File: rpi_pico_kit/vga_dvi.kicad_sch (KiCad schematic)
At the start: 21 parts, among them J4 DB15_Female_HighDensity_Mount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, J5 HDMI_A

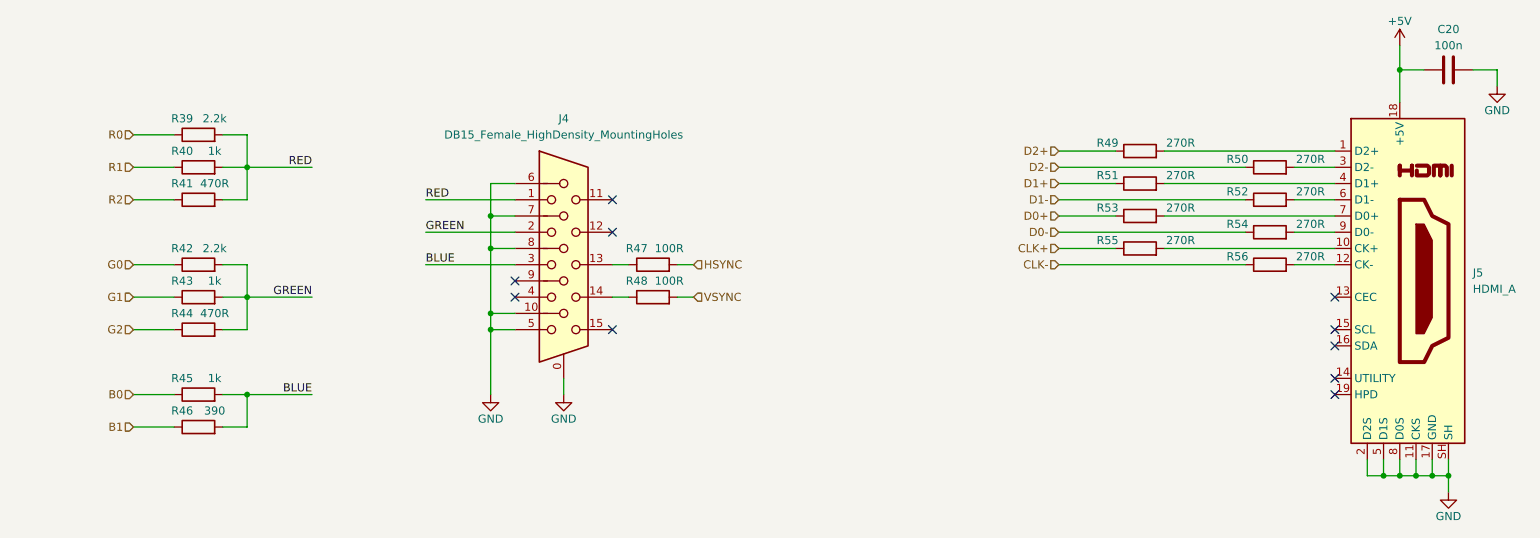
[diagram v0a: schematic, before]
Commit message: added i2c interface for vga and dvi
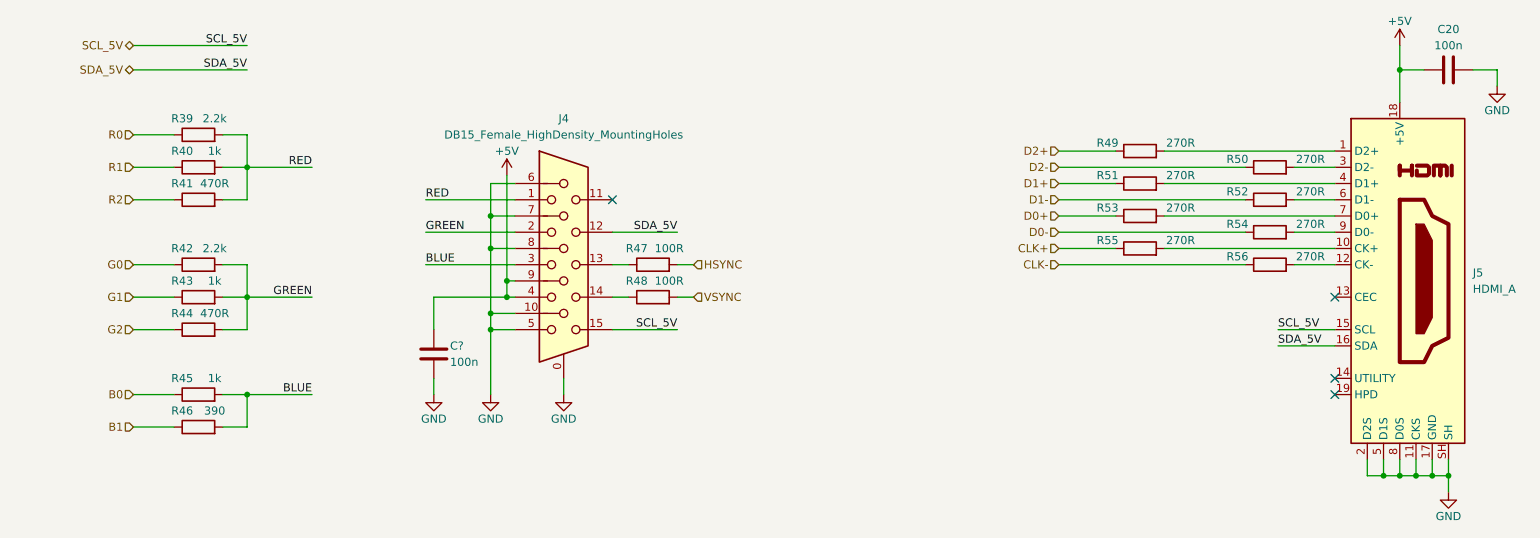
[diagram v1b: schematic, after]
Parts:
- added C?: 100n, Capacitor_SMD:C_0805_2012Metric_Pad1.18x1.45mm_HandSolder, symbol Device:C
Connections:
- net +5V: now also J4.4, J4.9, C?.2
- net GND: now also C?.1
- net SDA_5V: now reaches J4.12
- net SDA_5V: now also J5.16 (SDA)
- net SCL_5V: now reaches J4.15
- net SCL_5V: now also J5.15 (SCL)
- no-connect marks 10 -> 4
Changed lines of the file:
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@@
   (junction (at 251.46 123.19) (diameter 0) (color 0 0 0 0)
   )
+  (junction (at 104.14 92.71) (diameter 0) (color 0 0 0 0)
+  )
   (junction (at 248.92 123.19) (diameter 0) (color 0 0 0 0)
   )
   (junction (at 101.6 97.79) (diameter 0) (color 0 0 0 0)
   )
+  (junction (at 104.14 95.25) (diameter 0) (color 0 0 0 0)
+  )
   (junction (at 101.6 87.63) (diameter 0) (color 0 0 0 0)
   )
   (junction (at 63.5 95.25) (diameter 0) (color 0 0 0 0)
   )
-  (no_connect (at 233.68 100.33))
-  (no_connect (at 233.68 102.87))
   (no_connect (at 233.68 95.25))
   (no_connect (at 233.68 107.95))
   (no_connect (at 233.68 110.49))
-  (no_connect (at 105.41 95.25))
-  (no_connect (at 120.65 85.09))
-  (no_connect (at 105.41 92.71))
   (no_connect (at 120.65 80.01))
-  (no_connect (at 120.65 100.33))
+  (wire (pts (xy 120.65 85.09) (xy 130.81 85.09))
+    (stroke (width 0) (type default))
+  )
   (wire (pts (xy 227.33 80.01) (xy 233.68 80.01))
     (stroke (width 0) (type default))
@@
     (stroke (width 0) (type default))
   )
+  (wire (pts (xy 45.72 59.69) (xy 63.5 59.69))
+    (stroke (width 0) (type default))
+  )
   (wire (pts (xy 207.01 82.55) (xy 233.68 82.55))
     (stroke (width 0) (type default))
@@
     (stroke (width 0) (type default))
   )
+  (wire (pts (xy 224.79 102.87) (xy 233.68 102.87))
+    (stroke (width 0) (type default))
+  )
   (wire (pts (xy 248.92 120.65) (xy 248.92 123.19))
     (stroke (width 0) (type default))
@@
     (stroke (width 0) (type default))
   )
+  (wire (pts (xy 104.14 92.71) (xy 104.14 76.2))
+    (stroke (width 0) (type default))
+  )
   (wire (pts (xy 241.3 120.65) (xy 241.3 123.19))
     (stroke (width 0) (type default))
   )
+  (wire (pts (xy 92.71 95.25) (xy 104.14 95.25))
+    (stroke (width 0) (type default))
+  )
+  (wire (pts (xy 45.72 55.88) (xy 63.5 55.88))
+    (stroke (width 0) (type default))
+  )
   (wire (pts (xy 190.5 72.39) (xy 199.39 72.39))
     (stroke (width 0) (type default))
@@
     (stroke (width 0) (type default))
   )
+  (wire (pts (xy 104.14 95.25) (xy 104.14 92.71))
+    (stroke (width 0) (type default))
+  )
   (wire (pts (xy 251.46 120.65) (xy 251.46 123.19))
     (stroke (width 0) (type default))
@@
     (stroke (width 0) (type default))
   )
+  (wire (pts (xy 92.71 110.49) (xy 92.71 107.95))
+    (stroke (width 0) (type default))
+  )
+  (wire (pts (xy 105.41 95.25) (xy 104.14 95.25))
+    (stroke (width 0) (type default))
+  )
   (wire (pts (xy 63.5 74.93) (xy 73.66 74.93))
     (stroke (width 0) (type default))
@@
     (stroke (width 0) (type default))
   )
+  (wire (pts (xy 120.65 100.33) (xy 130.81 100.33))
+    (stroke (width 0) (type default))
+  )
   (wire (pts (xy 113.03 107.95) (xy 113.03 110.49))
     (stroke (width 0) (type default))
@@
     (stroke (width 0) (type default))
   )
+  (wire (pts (xy 224.79 100.33) (xy 233.68 100.33))
+    (stroke (width 0) (type default))
+  )
   (wire (pts (xy 59.69 115.57) (xy 63.5 115.57))
     (stroke (width 0) (type default))
@@
     (stroke (width 0) (type default))
   )
+  (wire (pts (xy 104.14 92.71) (xy 105.41 92.71))
+    (stroke (width 0) (type default))
+  )
   (wire (pts (xy 101.6 87.63) (xy 105.41 87.63))
+    (stroke (width 0) (type default))
+  )
+  (wire (pts (xy 92.71 100.33) (xy 92.71 95.25))
     (stroke (width 0) (type default))
   )
@@
     (effects (font (size 1.27 1.27)) (justify right bottom))
   )
+  (label "SCL_5V" (at 130.81 100.33 0) (fields_autoplaced)
+    (effects (font (size 1.27 1.27)) (justify right bottom))
+  )
+  (label "SDA_5V" (at 224.79 102.87 0) (fields_autoplaced)
+    (effects (font (size 1.27 1.27)) (justify left bottom))
+  )
   (label "BLUE" (at 91.44 90.17 0) (fields_autoplaced)
     (effects (font (size 1.27 1.27)) (justify left bottom))
@@
     (effects (font (size 1.27 1.27)) (justify left bottom))
   )
+  (label "SCL_5V" (at 224.79 100.33 0) (fields_autoplaced)
+    (effects (font (size 1.27 1.27)) (justify left bottom))
+  )
   (label "GREEN" (at 73.66 95.25 0) (fields_autoplaced)
     (effects (font (size 1.27 1.27)) (justify right bottom))
   )
+  (label "SCL_5V" (at 63.5 55.88 0) (fields_autoplaced)
+    (effects (font (size 1.27 1.27)) (justify right bottom))
+  )
+  (label "SDA_5V" (at 130.81 85.09 0) (fields_autoplaced)
+    (effects (font (size 1.27 1.27)) (justify right bottom))
+  )
   (label "RED" (at 73.66 74.93 0) (fields_autoplaced)
     (effects (font (size 1.27 1.27)) (justify right bottom))
   )
+  (label "SDA_5V" (at 63.5 59.69 0) (fields_autoplaced)
+    (effects (font (size 1.27 1.27)) (justify right bottom))
+  )
   (hierarchical_label "D1-" (shape input) (at 190.5 80.01 180) (fields_autoplaced)
     (effects (font (size 1.27 1.27)) (justify right))
@@
     (effects (font (size 1.27 1.27)) (justify right))
   )
+  (hierarchical_label "SDA_5V" (shape bidirectional) (at 45.72 59.69 180) (fields_autoplaced)
+    (effects (font (size 1.27 1.27)) (justify right))
+  )
   (hierarchical_label "R0" (shape input) (at 45.72 69.85 180) (fields_autoplaced)
     (effects (font (size 1.27 1.27)) (justify right))
@@
   )
   (hierarchical_label "G2" (shape input) (at 45.72 100.33 180) (fields_autoplaced)
+    (effects (font (size 1.27 1.27)) (justify right))
+  )
+  (hierarchical_label "SCL_5V" (shape bidirectional) (at 45.72 55.88 180) (fields_autoplaced)
     (effects (font (size 1.27 1.27)) (justify right))
   )
@@
     (pin "1")
   )
+  (symbol (lib_id "power:GND") (at 92.71 110.49 0) (unit 1)
+    (in_bom yes) (on_board yes)
+    (property "Reference" "#PWR?" (id 0) (at 92.71 116.84 0)
+      (effects (font (size 1.27 1.27)) hide)
+    )
+    (property "Value" "GND" (id 1) (at 92.71 114.3 0)
+      (effects (font (size 1.27 1.27)))
+    )
+    (property "Footprint" "" (id 2) (at 92.71 110.49 0)
+      (effects (font (size 1.27 1.27)) hide)
+    )
+    (property "Datasheet" "" (id 3) (at 92.71 110.49 0)
+      (effects (font (size 1.27 1.27)) hide)
+    )
+    (pin "1")
+  )
   (symbol (lib_id "Device:R") (at 223.52 74.93 90) (unit 1)
     (in_bom yes) (on_board yes)
@@
     (pin "2")
   )
+  (symbol (lib_id "Device:C") (at 92.71 104.14 180) (unit 1)
+    (in_bom yes) (on_board yes)
+    (property "Reference" "C?" (id 0) (at 95.25 102.87 0)
+      (effects (font (size 1.27 1.27)) (justify right))
+    )
+    (property "Value" "100n" (id 1) (at 95.25 105.41 0)
+      (effects (font (size 1.27 1.27)) (justify right))
+    )
+    (property "Footprint" "Capacitor_SMD:C_0805_2012Metric_Pad1.18x1.45mm_HandSolder" (id 2) (at 91.7448 100.33 0)
+      (effects (font (size 1.27 1.27)) hide)
+    )
+    (property "Datasheet" "~" (id 3) (at 92.71 104.14 0)
+      (effects (font (size 1.27 1.27)) hide)
+    )
+    (pin "1")
+    (pin "2")
+  )
   (symbol (lib_id "power:GND") (at 251.46 125.73 0) (unit 1)
     (in_bom yes) (on_board yes)
@@
     (pin "2")
   )
+  (symbol (lib_id "power:+5V") (at 104.14 76.2 0) (unit 1)
+    (in_bom yes) (on_board yes)
+    (property "Reference" "#PWR?" (id 0) (at 104.14 80.01 0)
+      (effects (font (size 1.27 1.27)) hide)
+    )
+    (property "Value" "+5V" (id 1) (at 104.14 72.39 0)
+      (effects (font (size 1.27 1.27)))
+    )
+    (property "Footprint" "" (id 2) (at 104.14 76.2 0)
+      (effects (font (size 1.27 1.27)) hide)
+    )
+    (property "Datasheet" "" (id 3) (at 104.14 76.2 0)
+      (effects (font (size 1.27 1.27)) hide)
+    )
+    (pin "1")
+  )
   (symbol (lib_id "Connector:HDMI_A") (at 243.84 92.71 0) (unit 1)

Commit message: added some footprints
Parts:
- gave numbers to parts that had none: 1
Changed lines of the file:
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@@
   (symbol (lib_id "power:GND") (at 92.71 110.49 0) (unit 1)
     (in_bom yes) (on_board yes)
-    (property "Reference" "#PWR?" (id 0) (at 92.71 116.84 0)
+    (property "Reference" "#PWR0146" (id 0) (at 92.71 116.84 0)
       (effects (font (size 1.27 1.27)) hide)
     )
@@
   (symbol (lib_id "Device:C") (at 92.71 104.14 180) (unit 1)
     (in_bom yes) (on_board yes)
-    (property "Reference" "C?" (id 0) (at 95.25 102.87 0)
+    (property "Reference" "C43" (id 0) (at 95.25 102.87 0)
       (effects (font (size 1.27 1.27)) (justify right))
     )
@@
   (symbol (lib_id "power:+5V") (at 104.14 76.2 0) (unit 1)
     (in_bom yes) (on_board yes)
-    (property "Reference" "#PWR?" (id 0) (at 104.14 80.01 0)
+    (property "Reference" "#PWR0147" (id 0) (at 104.14 80.01 0)
       (effects (font (size 1.27 1.27)) hide)
     )

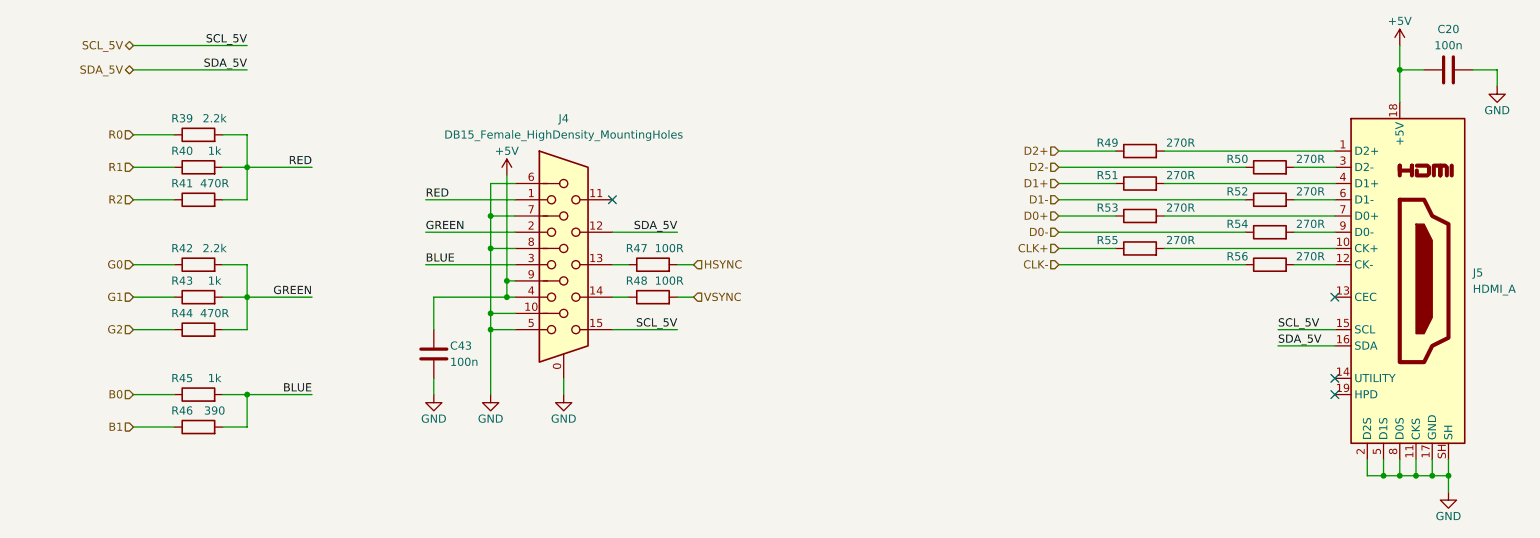
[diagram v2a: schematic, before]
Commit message: added jumpers to vga
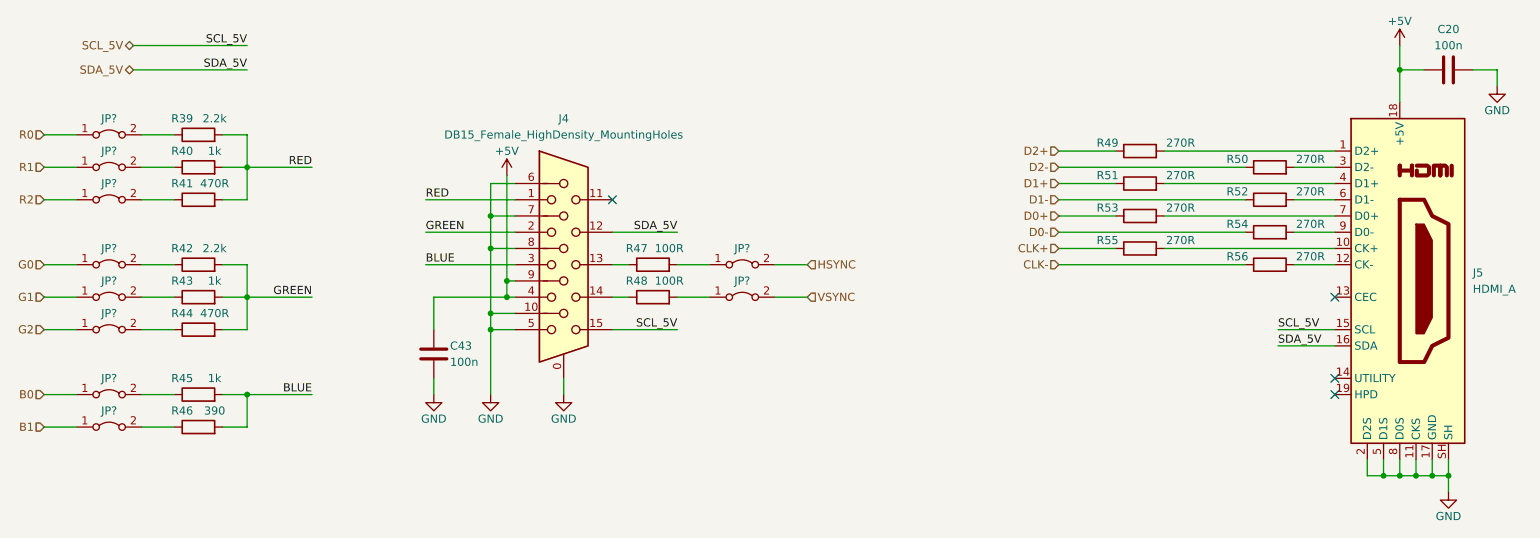
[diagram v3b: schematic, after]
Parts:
- added JP? (x10): Jumper_2_Bridged, TestPoint:TestPoint_2Pads_Pitch2.54mm_Drill0.8mm, symbol Jumper:Jumper_2_Bridged
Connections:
- net B0: now also JP?.1 (A); no longer R45.1
- net B1: now also JP?.1 (A); no longer R46.1
- net G0: now also JP?.1 (A); no longer R42.1
- net G1: now also JP?.1 (A); no longer R43.1
- net G2: now also JP?.1 (A); no longer R44.1
- net HSYNC: now also JP?.2 (B); no longer R47.2
- net R0: now also JP?.1 (A); no longer R39.1
- net R1: now also JP?.1 (A); no longer R40.1
- net R2: now also JP?.1 (A); no longer R41.1
- net VSYNC: now also JP?.2 (B); no longer R48.2
- new net: JP?.1 (A), R47.2
- new net: JP?.2 (B), R44.1
- new net: JP?.2 (B), R43.1
- new net: JP?.1 (A), R48.2
- new net: JP?.2 (B), R39.1
- new net: JP?.2 (B), R46.1
- new net: JP?.2 (B), R45.1
- new net: JP?.2 (B), R41.1
- new net: JP?.2 (B), R42.1
- new net: JP?.2 (B), R40.1

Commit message: added test pads for uart and swd of debugger
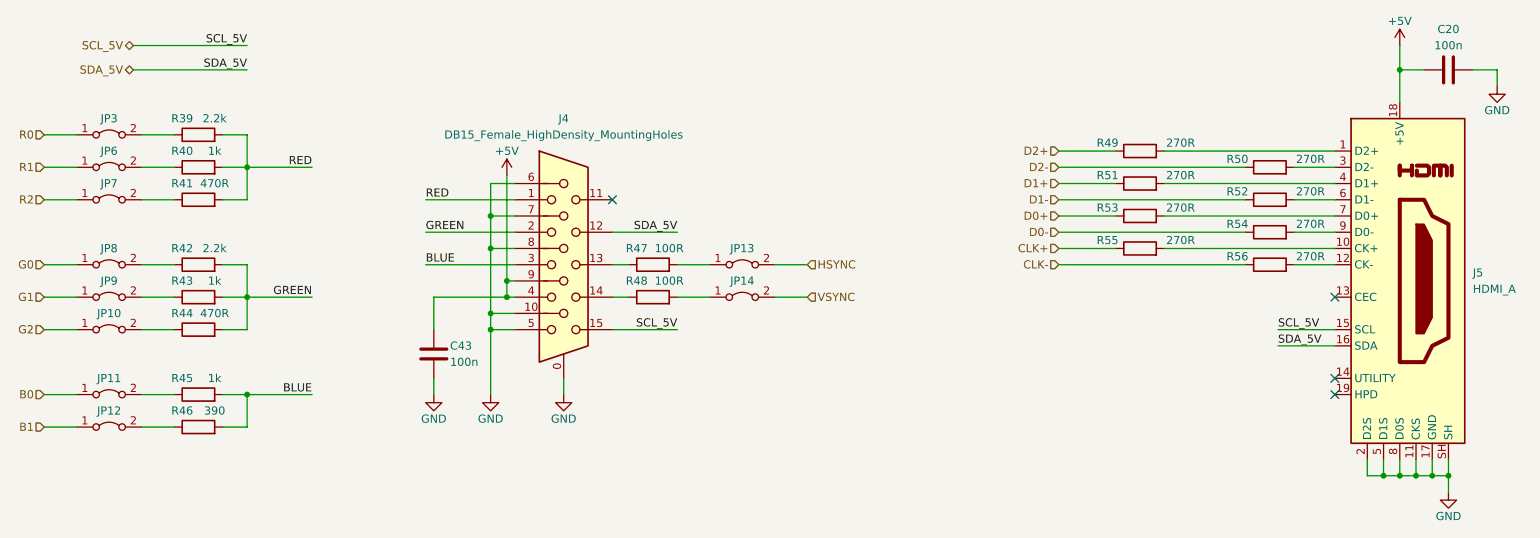
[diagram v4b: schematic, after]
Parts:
- gave numbers to parts that had none: 10
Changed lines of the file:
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@@
   (symbol (lib_id "Jumper:Jumper_2_Bridged") (at 140.97 90.17 0) (unit 1)
     (in_bom yes) (on_board yes) (fields_autoplaced)
-    (property "Reference" "JP?" (id 0) (at 140.97 87.63 0)
+    (property "Reference" "JP13" (id 0) (at 140.97 87.63 0)
       (effects (font (size 1.27 1.27)))
     )
@@
   (symbol (lib_id "Jumper:Jumper_2_Bridged") (at 41.91 115.57 0) (unit 1)
     (in_bom yes) (on_board yes) (fields_autoplaced)
-    (property "Reference" "JP?" (id 0) (at 41.91 113.03 0)
+    (property "Reference" "JP12" (id 0) (at 41.91 113.03 0)
       (effects (font (size 1.27 1.27)))
     )
@@
   (symbol (lib_id "Jumper:Jumper_2_Bridged") (at 41.91 95.25 0) (unit 1)
     (in_bom yes) (on_board yes) (fields_autoplaced)
-    (property "Reference" "JP?" (id 0) (at 41.91 92.71 0)
+    (property "Reference" "JP9" (id 0) (at 41.91 92.71 0)
       (effects (font (size 1.27 1.27)))
     )
@@
   (symbol (lib_id "Jumper:Jumper_2_Bridged") (at 41.91 100.33 0) (unit 1)
     (in_bom yes) (on_board yes) (fields_autoplaced)
-    (property "Reference" "JP?" (id 0) (at 41.91 97.79 0)
+    (property "Reference" "JP10" (id 0) (at 41.91 97.79 0)
       (effects (font (size 1.27 1.27)))
     )
@@
   (symbol (lib_id "Jumper:Jumper_2_Bridged") (at 41.91 80.01 0) (unit 1)
     (in_bom yes) (on_board yes) (fields_autoplaced)
-    (property "Reference" "JP?" (id 0) (at 41.91 77.47 0)
+    (property "Reference" "JP7" (id 0) (at 41.91 77.47 0)
       (effects (font (size 1.27 1.27)))
     )
@@
   (symbol (lib_id "Jumper:Jumper_2_Bridged") (at 41.91 69.85 0) (unit 1)
     (in_bom yes) (on_board yes) (fields_autoplaced)
-    (property "Reference" "JP?" (id 0) (at 41.91 67.31 0)
+    (property "Reference" "JP3" (id 0) (at 41.91 67.31 0)
       (effects (font (size 1.27 1.27)))
     )
@@
   (symbol (lib_id "Jumper:Jumper_2_Bridged") (at 140.97 95.25 0) (unit 1)
     (in_bom yes) (on_board yes) (fields_autoplaced)
-    (property "Reference" "JP?" (id 0) (at 140.97 92.71 0)
+    (property "Reference" "JP14" (id 0) (at 140.97 92.71 0)
       (effects (font (size 1.27 1.27)))
     )
@@
   (symbol (lib_id "Jumper:Jumper_2_Bridged") (at 41.91 74.93 0) (unit 1)
     (in_bom yes) (on_board yes) (fields_autoplaced)
-    (property "Reference" "JP?" (id 0) (at 41.91 72.39 0)
+    (property "Reference" "JP6" (id 0) (at 41.91 72.39 0)
       (effects (font (size 1.27 1.27)))
     )
@@
   (symbol (lib_id "Jumper:Jumper_2_Bridged") (at 41.91 110.49 0) (unit 1)
     (in_bom yes) (on_board yes) (fields_autoplaced)
-    (property "Reference" "JP?" (id 0) (at 41.91 107.95 0)
+    (property "Reference" "JP11" (id 0) (at 41.91 107.95 0)
       (effects (font (size 1.27 1.27)))
     )
@@
   (symbol (lib_id "Jumper:Jumper_2_Bridged") (at 41.91 90.17 0) (unit 1)
     (in_bom yes) (on_board yes) (fields_autoplaced)
-    (property "Reference" "JP?" (id 0) (at 41.91 87.63 0)
-      (effects (font (size 1.27 1.27)))
-    )
+    (property "Reference" "JP8" (id 0) (at 41.91 87.63 0)
+      (effects (font (size 1.27 1.27)))
+    )
